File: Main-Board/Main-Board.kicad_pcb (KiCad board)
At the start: 2 copper layers, 76.2 x 76.2 mm, 59 parts, among them J1 Power In, J2 ESC_1, J3 ESC_2, J4 ESC_3, J5 ESC_4, J6 USB_B_Micro, J7 ICSP, Q1 BSS138, Q2 BSS138, U1 MCP6001U, U2 ICM-20689, U3 FT232RL, U4 ATmega328P-AU, U5 LM1117-5.0, Y1 16 MHz

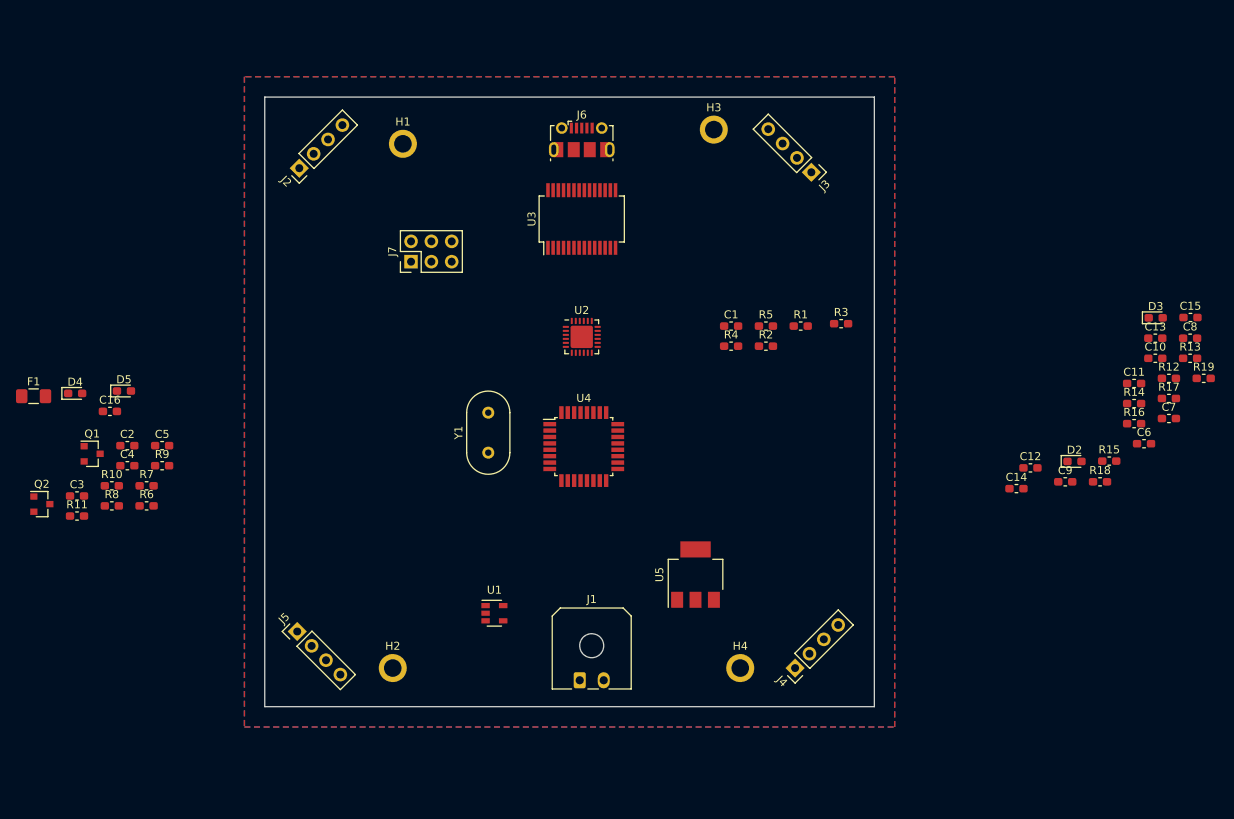
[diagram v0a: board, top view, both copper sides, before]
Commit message: Everything is in the schematic. Just need to review board then start the layout. Printed off hard copy
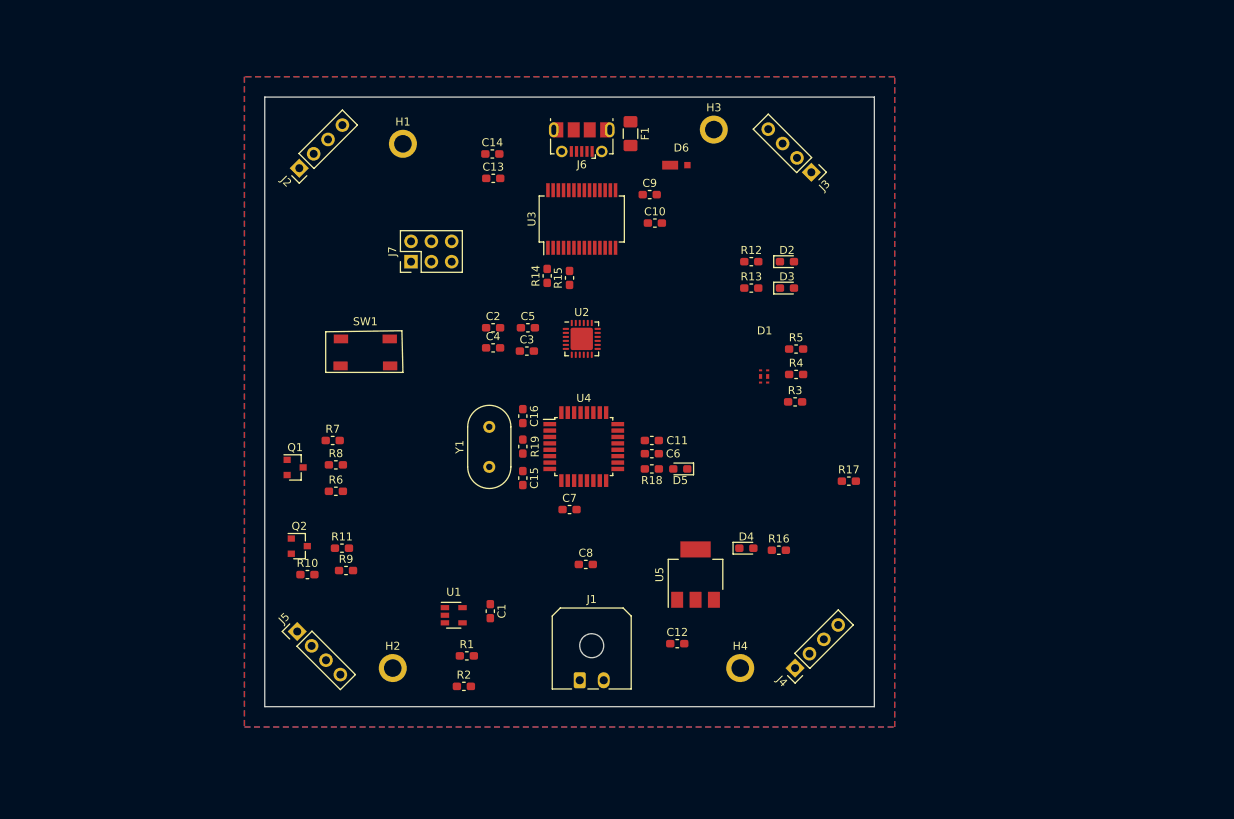
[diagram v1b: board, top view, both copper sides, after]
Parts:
- added D1: LED_RGB, Custom:RGB_LED, F.Cu at (113.2, 111.1)
- added D6: SS1P3L, Custom:SS1P3L, F.Cu at (102.9, 84.7)
- added SW1: Reset, Custom:Switch, F.Cu at (63.4, 108.0)
- moved D4 86.1 mm to (111.0, 132.6)
- moved C15 85.8 mm to (83.1, 123.8), turned to 270 degrees
- moved R19 85.5 mm to (83.1, 119.9), turned to 90 degrees
- moved C13 85.1 mm to (79.4, 86.4)
- moved F1 81.5 mm to (96.5, 80.8), turned to 270 degrees
- moved C8 80.7 mm to (90.9, 134.6)
- moved C14 77.7 mm to (79.2, 83.3)
- moved C7 75.8 mm to (88.9, 127.8)
- moved R14 75.1 mm to (86.1, 98.6), turned to 90 degrees
- moved R15 71.2 mm to (88.9, 98.8), turned to 90 degrees
- moved D5 70.2 mm to (102.7, 122.7), turned to 180 degrees
- moved C10 64.8 mm to (99.6, 91.9)
- moved C9 63.1 mm to (98.9, 88.4)
- moved C6 61.5 mm to (99.2, 120.8), turned to 180 degrees
- moved C11 60.7 mm to (99.2, 119.1)
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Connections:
- R3 pad 2: (no net) -> Net-(D1-Pad1)
- R4 pad 2: (no net) -> Net-(D1-Pad3)
- R5 pad 2: (no net) -> Net-(D1-Pad5)

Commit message: Checked over page one, biggest question is what connectors to use
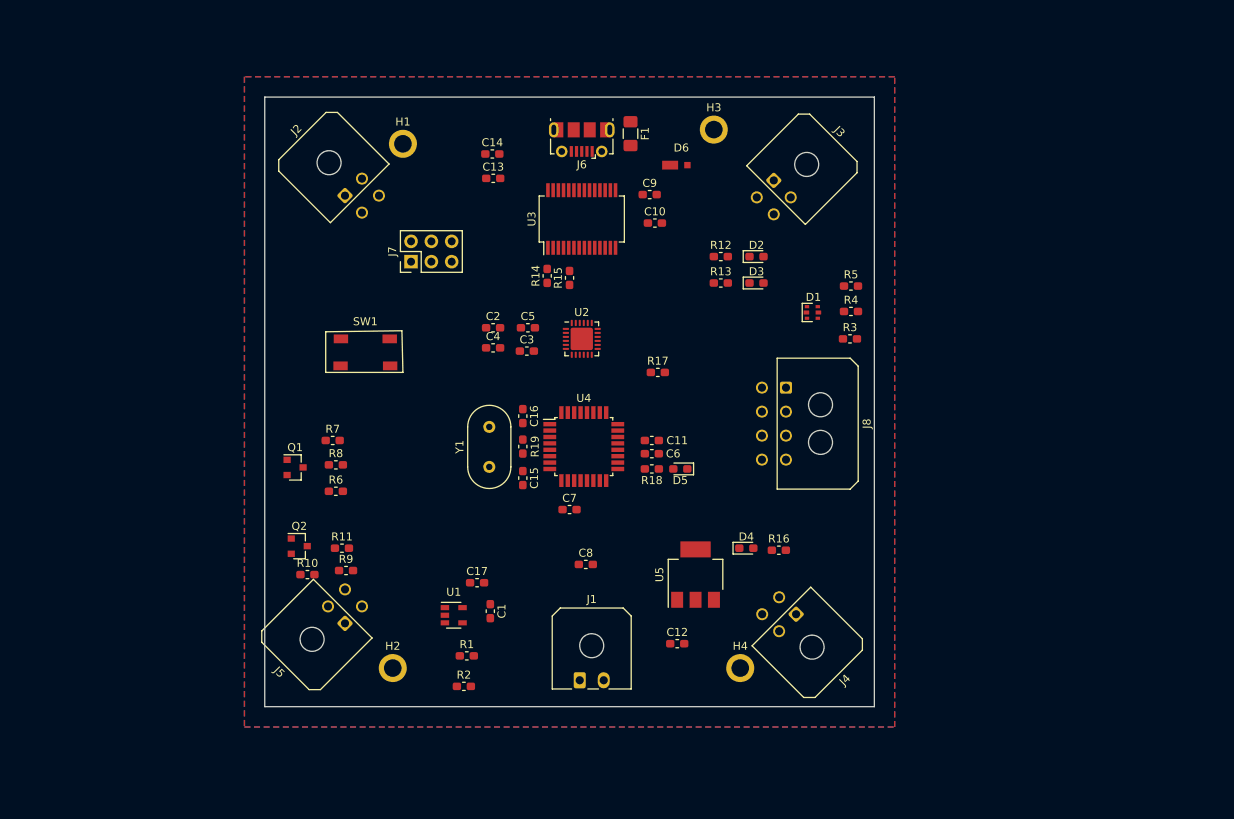
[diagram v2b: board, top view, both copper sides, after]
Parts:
- added C17: 1uF 16V X7R 20%, Capacitor_SMD:C_0603_1608Metric_Pad1.05x0.95mm_HandSolder, F.Cu at (77.3, 136.9)
- added J8: Receiver, Connector_Molex:Molex_Micro-Fit_3.0_43045-0800_2x04_P3.00mm_Horizontal, F.Cu at (116.0, 112.5)
- C1: value X7R, 0.1uF 10% -> 0.1uF 16V X7R 10%
- J2, J3, J4, J5: footprint Connector_PinHeader_2.54mm:PinHeader_1x04_P2.54mm_Vertical -> Connector_Molex:Molex_Micro-Fit_3.0_43045-0400_2x02_P3.00mm_Horizontal
- R1: value ?? kOhm 1% -> 3.2 kohm 1%
- R2: value ?? kOhm 1% -> 2 kohm 1%
- R3, R5: value ?? ohm 5% -> 87.5 ohm 5%
- R4: value ?? ohm 5% -> 147.5 ohm 5%
- moved R17 27.5 mm to (99.9, 110.6)
- moved R3 10.4 mm to (124.0, 106.4)
- moved R4 10.4 mm to (124.1, 103.0)
- moved R5 10.4 mm to (124.1, 99.8)
- moved D1 10.1 mm to (119.3, 103.1)
- moved J4 6.73 mm to (117.2, 140.8), turned to 225 degrees
- moved J2 6.66 mm to (60.8, 88.5), turned to 45 degrees
- moved J5 6.05 mm to (60.8, 142.0), turned to 135 degrees
- moved J3 4.81 mm to (114.4, 86.6), turned to 315 degrees
- moved D2 3.86 mm to (112.3, 96.1)
- moved R12 3.86 mm to (107.8, 96.1)
- moved D3 3.86 mm to (112.3, 99.4)
- moved R13 3.86 mm to (107.8, 99.4)
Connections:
- C1 pad 1: +5V -> GND
- C1 pad 2: GND -> +5V
- J7 pad 6: B_LED -> D12
- R3 pad 1: B_LED -> B_RGB_LED
- R4 pad 1: D2 -> (no net)
- R5 pad 1: D3 -> D2
- U4 pad 1: D3 -> B_RGB_LED
- U4 pad 12: (no net) -> D8
- U4 pad 13: (no net) -> D9
- U4 pad 14: (no net) -> D10
- U4 pad 16: B_LED -> D12

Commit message: Change to JST-GH connectors
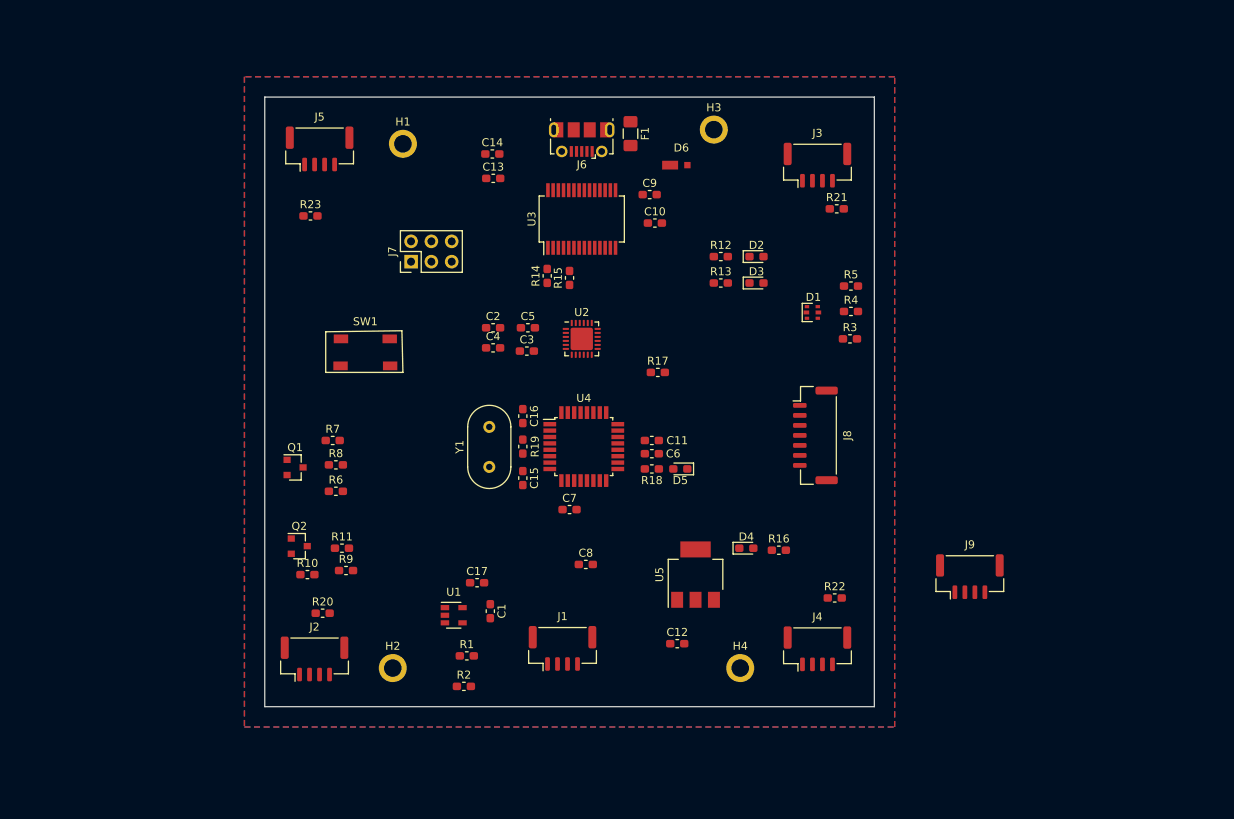
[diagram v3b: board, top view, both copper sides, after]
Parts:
- added J9: Aux, Connector_JST:JST_GH_BM04B-GHS-TBT_1x04-1MP_P1.25mm_Vertical, F.Cu at (138.9, 136.1)
- added R20: ?? ohm 5%, Resistor_SMD:R_0603_1608Metric_Pad1.05x0.95mm_HandSolder, F.Cu at (58.0, 140.7)
- added R21: ?? ohm 5%, Resistor_SMD:R_0603_1608Metric_Pad1.05x0.95mm_HandSolder, F.Cu at (122.3, 90.2)
- added R22: ?? ohm 5%, Resistor_SMD:R_0603_1608Metric_Pad1.05x0.95mm_HandSolder, F.Cu at (122.0, 138.8)
- added R23: ?? ohm 5%, Resistor_SMD:R_0603_1608Metric_Pad1.05x0.95mm_HandSolder, F.Cu at (56.5, 91.1)
- J1: value Power In -> Power_In; footprint Connector_Molex:Molex_Micro-Fit_3.0_43650-0200_1x02_P3.00mm_Horizontal -> Connector_JST:JST_GH_BM04B-GHS-TBT_1x04-1MP_P1.25mm_Vertical
- J2, J3, J4, J5: footprint Connector_Molex:Molex_Micro-Fit_3.0_43045-0400_2x02_P3.00mm_Horizontal -> Connector_JST:JST_GH_BM04B-GHS-TBT_1x04-1MP_P1.25mm_Vertical
- J8: footprint Connector_Molex:Molex_Micro-Fit_3.0_43045-0800_2x04_P3.00mm_Horizontal -> Connector_JST:JST_GH_BM07B-GHS-TBT_1x07-1MP_P1.25mm_Vertical
- moved J5 59.4 mm to (57.7, 82.7), turned to 0 degrees
- moved J2 58.0 mm to (57.0, 146.4), turned to 0 degrees
- moved J8 7.01 mm to (119.6, 118.5)
- moved J3 5.78 mm to (119.9, 84.7), turned to 0 degrees
- moved J4 5.08 mm to (119.9, 145.2), turned to 0 degrees
- moved J1 4.52 mm to (88.0, 145.1)
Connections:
- net D13 renamed Aux_Digital
- J1 pad 2: VDD -> GND
- J2 pad 2: A1 -> Net-(J2-Pad2)
- J3 pad 2: A2 -> Net-(J3-Pad2)
- J4 pad 2: A3 -> Net-(J4-Pad2)
- J5 pad 2: (no net) -> Net-(J5-Pad2)
- U4 pad 19: (no net) -> A6

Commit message: Reviewed MCU. Next have to generate BOM and route board
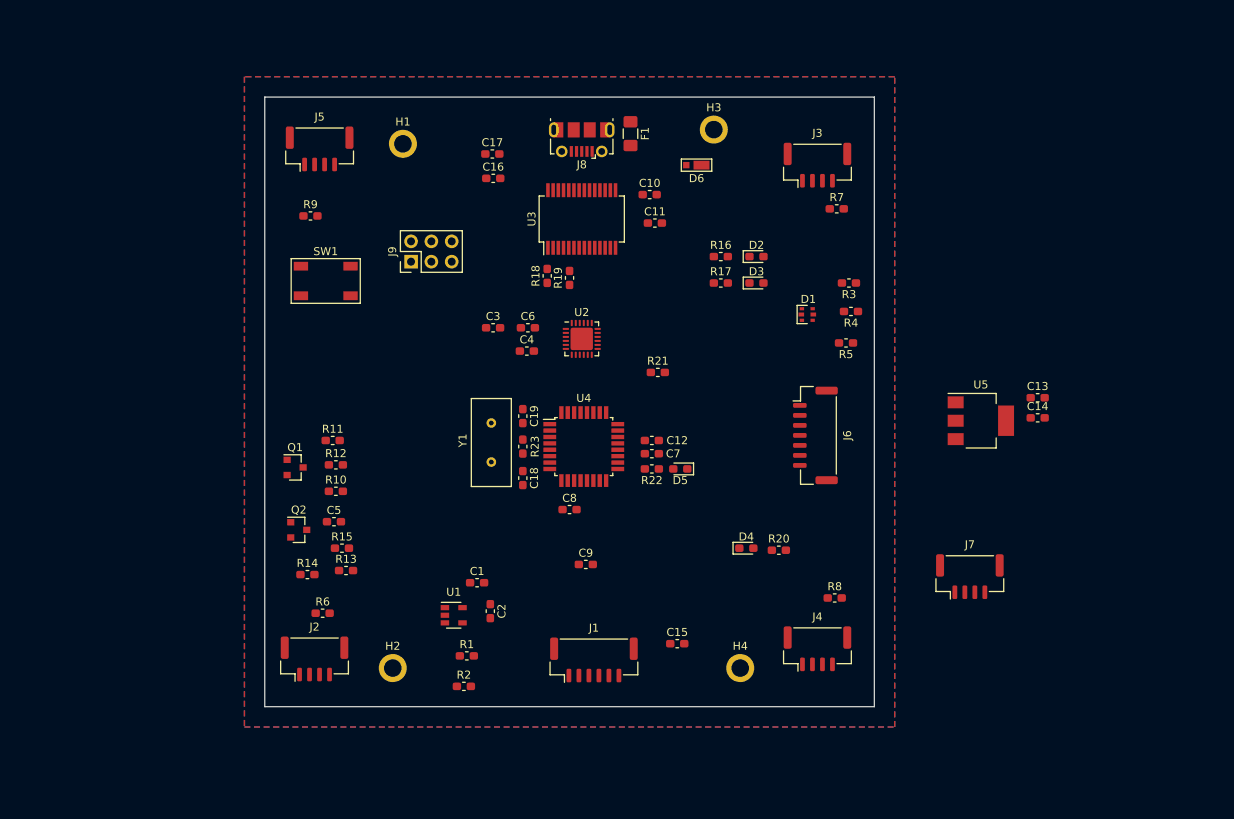
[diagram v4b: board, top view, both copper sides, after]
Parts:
- removed the C4 at (79.3, 107.5)
- added C13: 10uF 25V 20%, Capacitor_SMD:C_0603_1608Metric_Pad1.05x0.95mm_HandSolder, F.Cu at (147.4, 113.8)
- added C14: 10uF 25V 20%, Capacitor_SMD:C_0603_1608Metric_Pad1.05x0.95mm_HandSolder, F.Cu at (147.4, 116.3)
- added C5: 0.1uF 16V X7R 10%, Capacitor_SMD:C_0603_1608Metric_Pad1.05x0.95mm_HandSolder, F.Cu at (59.5, 129.3)
- C10: renamed from C9; value X7R, 100nF 10% -> 0.1uF 16V X7R 10%
- C11: renamed from C10; value X7R, 100nF 10% -> 0.1uF 16V X7R 10%
- C15: renamed from C12; value X7R, 1uF 10% -> 1uF 16V X7R 10%
- C17: renamed from C14; value X7R, 100nF 10% -> 0.1F 16V X7R 10%
- C18: renamed from C15; value X7R, 2pF 2% -> 2pF 16V X7R 2%
- C19: renamed from C16; value X7R, 2pF 2% -> 2pF 16V X7R 2%
- C3: renamed from C2; value X7R, 10nF 10% -> 10nF 16V X7R 10%
- C4: renamed from C3; value X7R, 2.2uF 10% -> 2.2uF 16V X7R 10%
- C6: renamed from C5; value X7R, 0.47uF 10% -> 0.47uF 16V X7R 10%
- C7: renamed from C6; value X7R, 1uF 10% -> 1uF 16V X7R 10%
- C9: renamed from C8; value X7R, 1uF 10% -> 1uF 16V X7R 10%
- J1: footprint Connector_JST:JST_GH_BM04B-GHS-TBT_1x04-1MP_P1.25mm_Vertical -> Connector_JST:JST_GH_BM06B-GHS-TBT_1x06-1MP_P1.25mm_Vertical
- R10: renamed from R6; value 10 kOhm 5% -> 10 kohm 5%
- R11: renamed from R7; value 10 kOhm 5% -> 10 kohm 5%
- R12: renamed from R8; value 10 kOhm 5% -> 10 kohm 5%
- R13: renamed from R9; value 10 kOhm 5% -> 10 kohm 5%
- R14: renamed from R10; value 10 kOhm 5% -> 10 kohm 5%
- R15: renamed from R11; value 10 kOhm 5% -> 10 kohm 5%
- R18: renamed from R14; value 1 kohm -> 1 kohm 5%
- R19: renamed from R15; value 1 kohm -> 1 kohm 5%
- R21: renamed from R17; value 10 kOhm 5% -> 1 kohm 5%
- Y1: footprint Crystal:Resonator-2Pin_W10.0mm_H5.0mm -> Custom:Crystal
- moved U5 40.5 mm to (140.3, 116.7), turned to 0 degrees
- moved SW1 10.1 mm to (58.4, 99.2)
- moved R5 7.14 mm to (123.5, 106.9), turned to 180 degrees
- moved R3 6.99 mm to (123.8, 99.4), turned to 180 degrees
- moved J1 4.18 mm to (91.9, 146.6)
- moved Y1 3.06 mm to (79.1, 119.4)
- moved Q2 2.04 mm to (55.1, 130.3)
- moved D6 1.27 mm to (104.1, 84.7), turned to 180 degrees
- moved D1 0.68 mm to (118.6, 103.4)
- turned R4 to 180 degrees
- renumbered C17 to C1, C11 to C12, C13 to C16, C1 to C2, C7 to C8, J8 to J6, J9 to J7, J6 to J8, J7 to J9, R12 to R16, R13 to R17, R16 to R20, R18 to R22, R19 to R23, R20 to R6, R21 to R7, R22 to R8, R23 to R9
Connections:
- J1 pad 3: VDD -> GND
- U5 pad 4: (no net) -> +5V

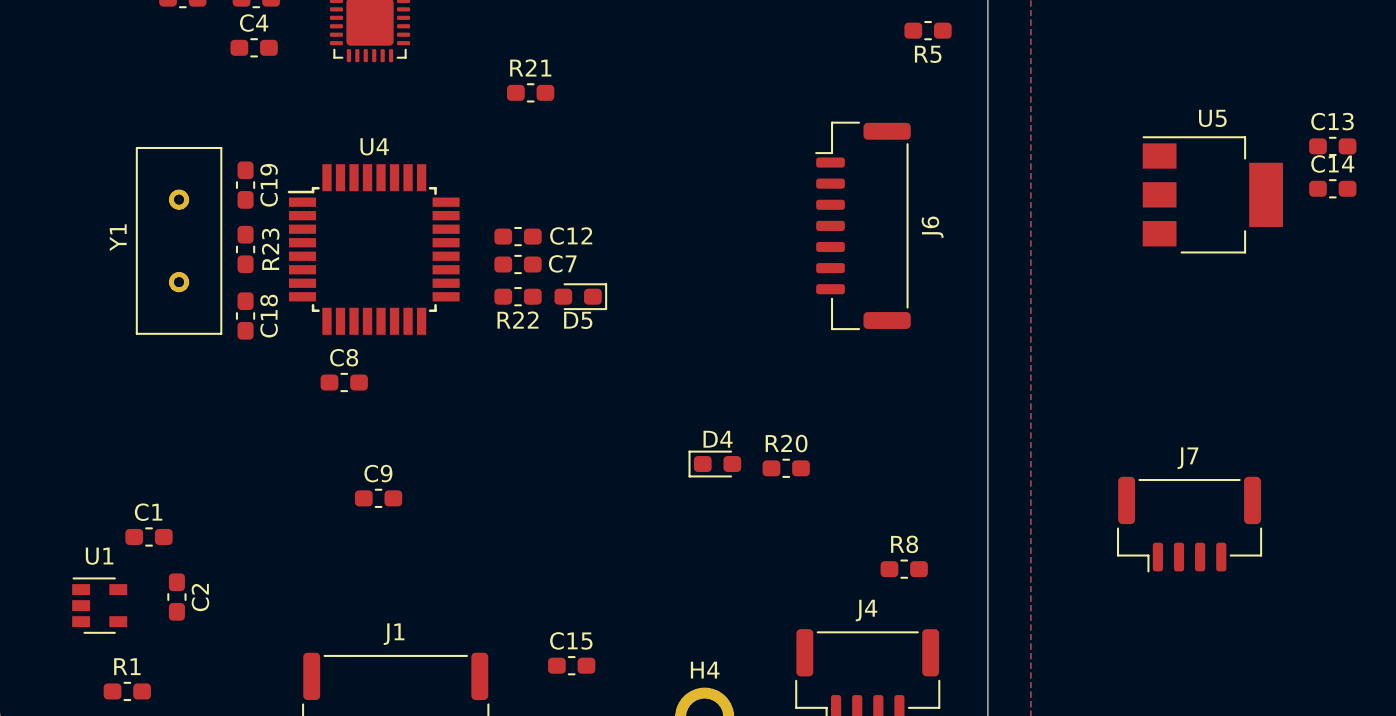
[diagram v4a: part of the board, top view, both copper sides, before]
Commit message: Switched from crystal to Resonator
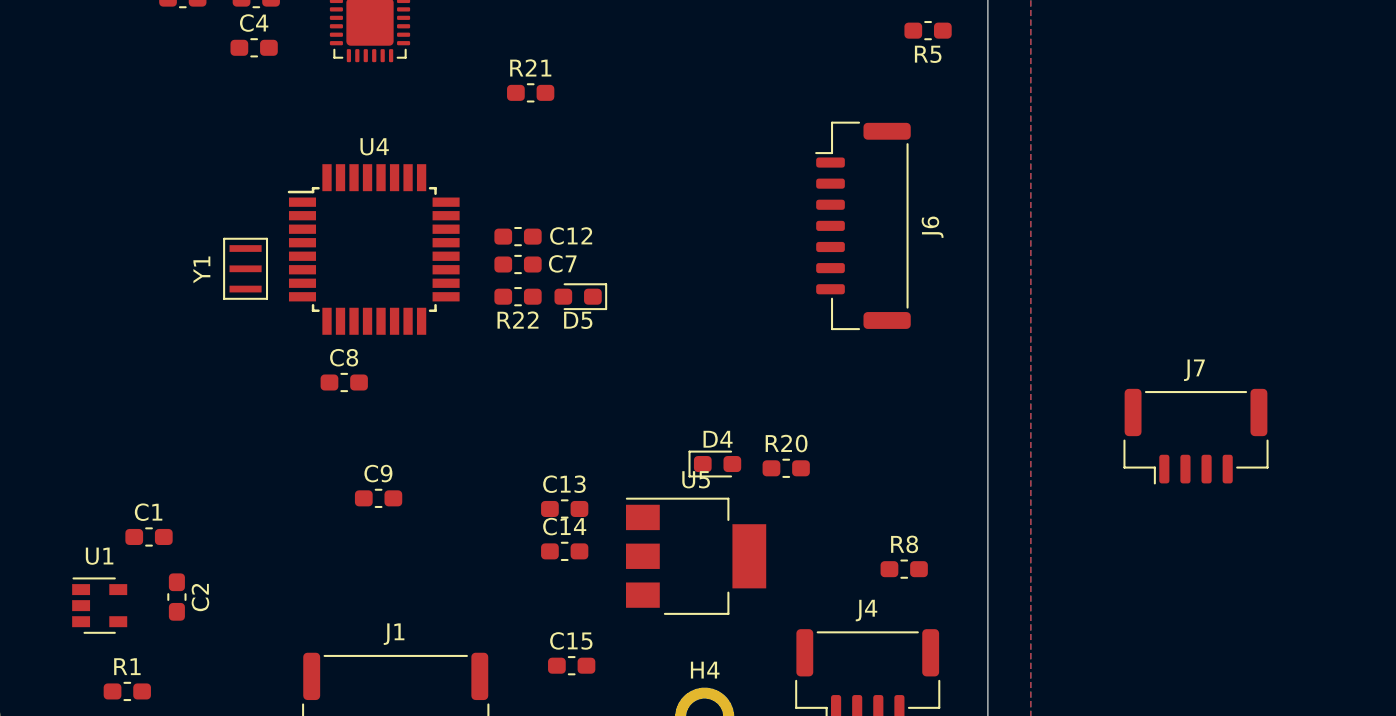
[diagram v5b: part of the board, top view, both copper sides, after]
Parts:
- removed C18, C19: 2pF 16V X7R 2%, Capacitor_SMD:C_0603_1608Metric_Pad1.05x0.95mm_HandSolder
- removed R23: 1 Mohm, Resistor_SMD:R_0603_1608Metric_Pad1.05x0.95mm_HandSolder
- C1: value 1uF 16V X7R 20% -> 1uF 16V X7R 10%
- C12: value X7R, 100nF 10% -> 0.1uF 16V X7R 10%
- C16: value 4.7uF 16V 20% -> 4.7uF 10V 20%
- C17: value 0.1F 16V X7R 10% -> 0.1uF 16V X7R 10%
- C8: value 4.7uF 16V -> 4.7uF 10V 20%
- R16, R17, R22: value 200 ohm -> 200 ohm 5%
- R20: value 140 ohm -> 150 ohm 5%
- R3, R5: value 87.5 ohm 5% -> 100 ohm 5%
- R4: value 147.5 ohm 5% -> 150 ohm 5%
- Y1: footprint Custom:Crystal -> Custom:Resonator
- moved C14 50.3 mm to (101.9, 137.8)
- moved C13 50.3 mm to (101.9, 135.2)
- moved U5 37.3 mm to (109.7, 138.0)
- moved J7 5.22 mm to (139.3, 130.9)
- moved Y1 4.27 mm to (83.1, 121.0)
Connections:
- U4 pad 7: XTAL1 -> Net-(U4-Pad7)
- U4 pad 8: XTAL2 -> Net-(U4-Pad8)
- Y1 pad 1: XTAL1 -> Net-(U4-Pad8)
- Y1 pad 2: XTAL2 -> GND
